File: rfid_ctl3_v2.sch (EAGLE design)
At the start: 45 parts, among them Q1 FDS5680, Q2 FDS5680, SW2 L202011MS02Q, U1 MC34063SMD

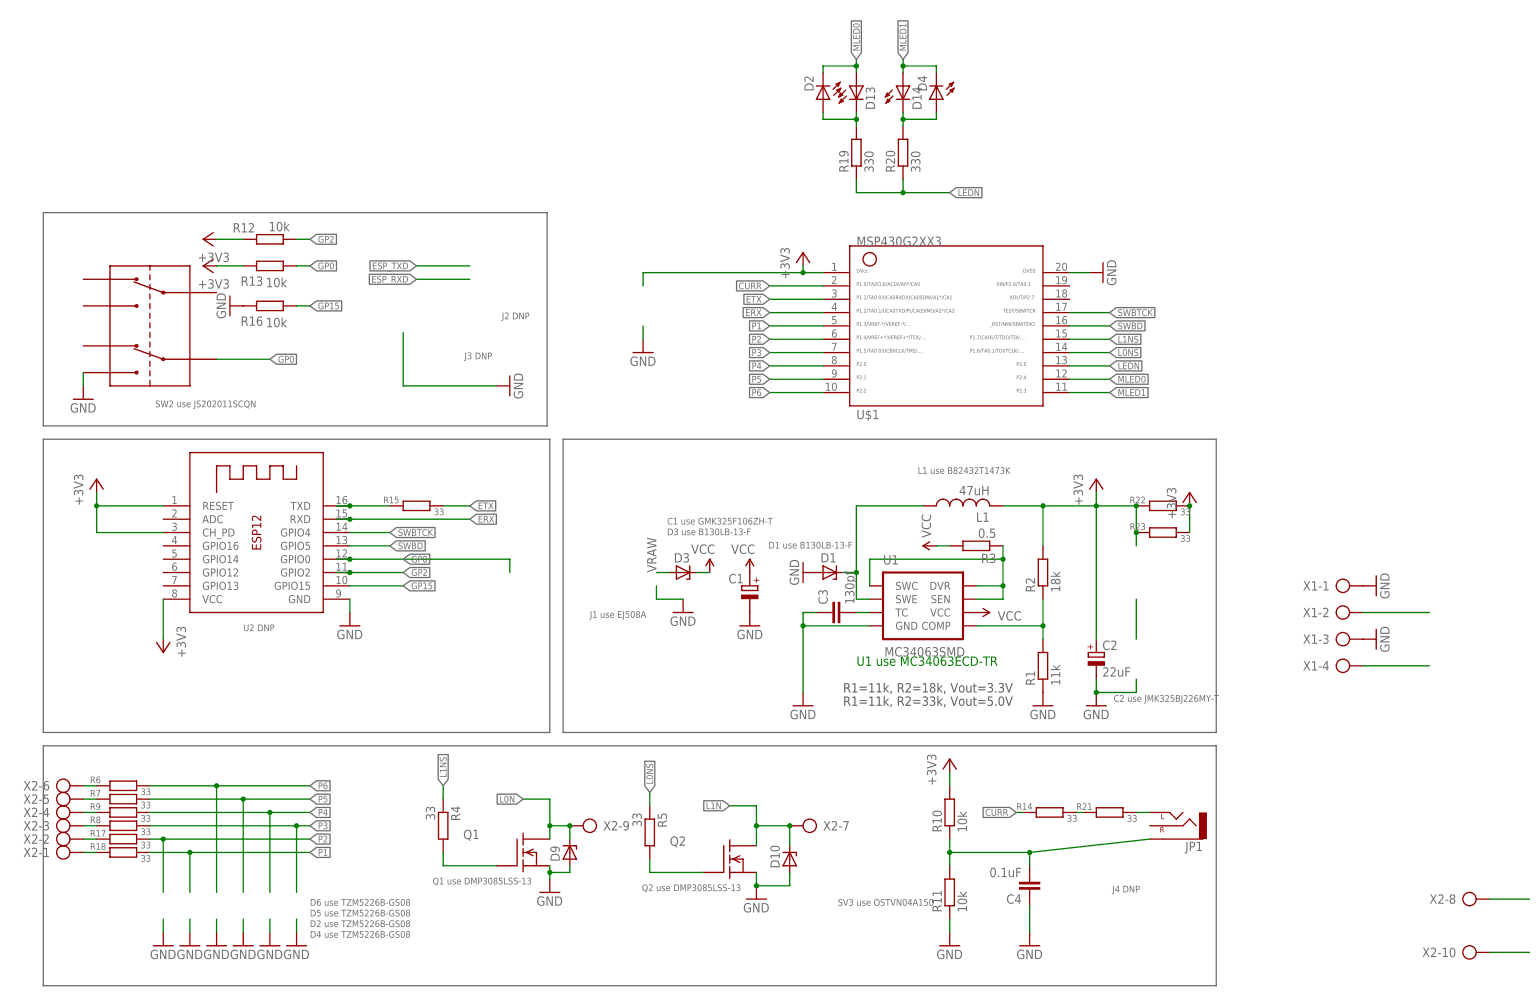
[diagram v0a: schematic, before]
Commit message: cleaned up schem and added schematic png
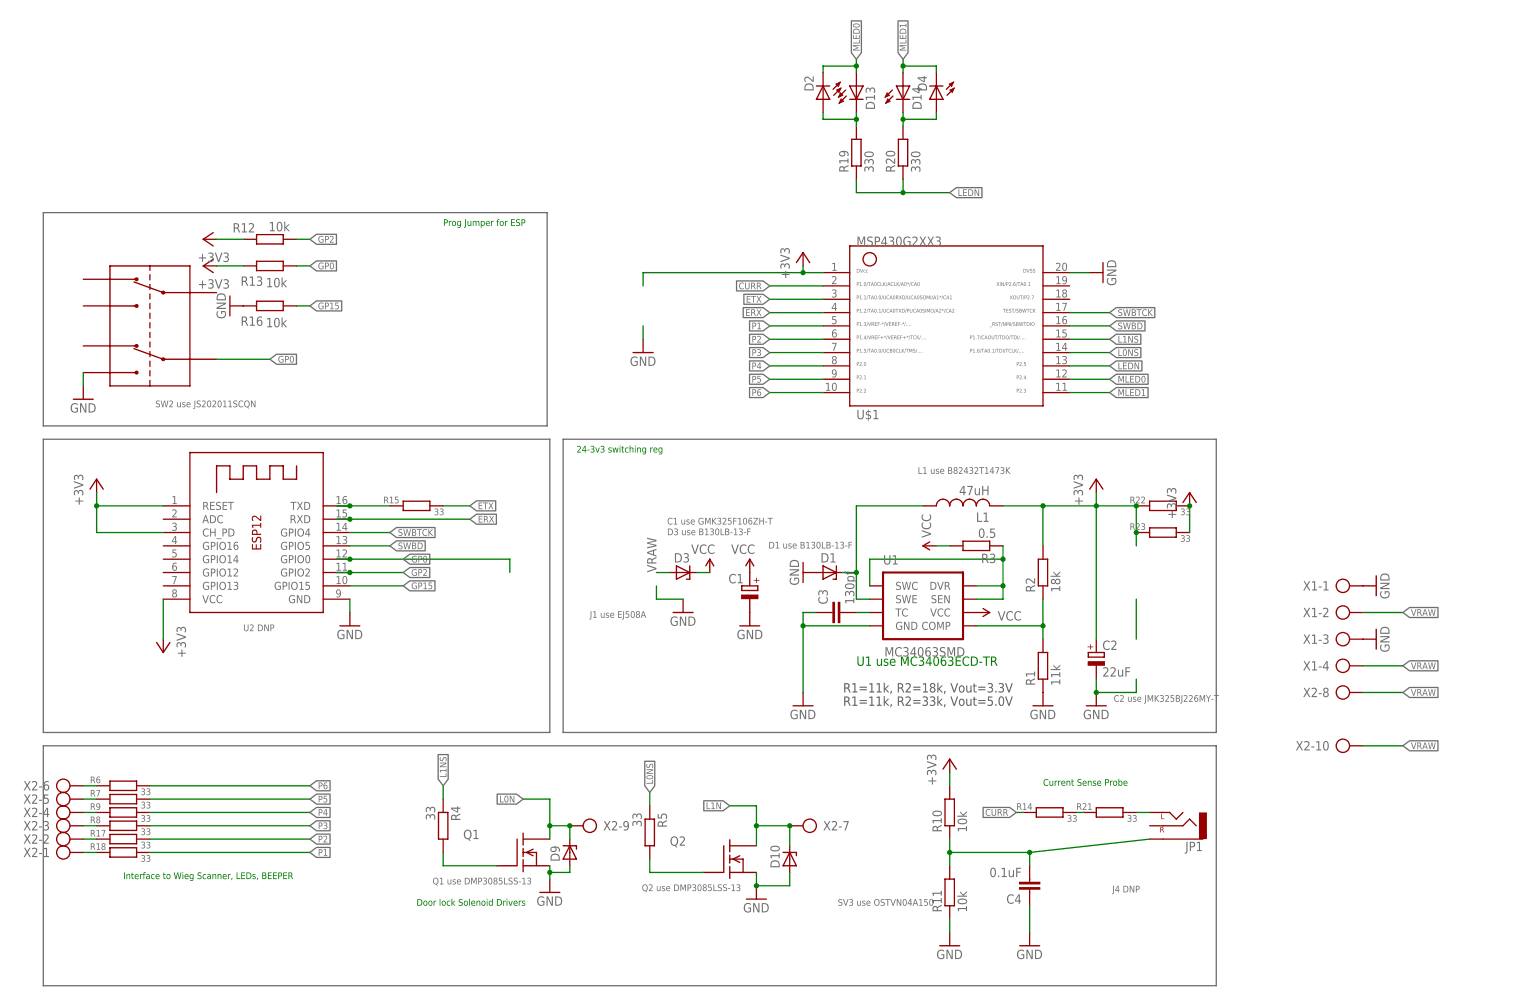
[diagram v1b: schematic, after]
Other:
- note added: "24-3v3 switching reg"
- note added: "Current Sense Probe"
- note added: "Door lock Solenoid Drivers"
- note added: "Interface to Wieg Scanner, LEDs, BEEPER"
- note added: "Prog Jumper for ESP"
- note removed: "D2 use TZM5226B-GS08"
- note removed: "D4 use TZM5226B-GS08"
- note removed: "D5 use TZM5226B-GS08"
- note removed: "D6 use TZM5226B-GS08"
- note removed: "J2 DNP"
- note removed: "J3 DNP"
- moved on the sheet: X2-10, X2-8
